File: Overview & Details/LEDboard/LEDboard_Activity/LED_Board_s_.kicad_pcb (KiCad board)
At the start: 2 copper layers, 0 parts

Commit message: Place components
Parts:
- added D1: APA102-2020, LED_SMD:LED-APA102-2020, F.Cu at (69.4, 47.9)
- added D10: APA102-2020, LED_SMD:LED-APA102-2020, F.Cu at (104.3, 57.5)
- added D11: APA102-2020, LED_SMD:LED-APA102-2020, F.Cu at (86.8, 57.5)
- added D12: APA102-2020, LED_SMD:LED-APA102-2020, F.Cu at (69.4, 57.5)
- added D13: APA102-2020, LED_SMD:LED-APA102-2020, F.Cu at (69.4, 67.0)
- added D14: APA102-2020, LED_SMD:LED-APA102-2020, F.Cu at (86.8, 67.0)
- added D15: APA102-2020, LED_SMD:LED-APA102-2020, F.Cu at (104.3, 67.0)
- added D16: APA102-2020, LED_SMD:LED-APA102-2020, F.Cu at (121.8, 67.0)
- added D17: APA102-2020, LED_SMD:LED-APA102-2020, F.Cu at (139.2, 67.0)
- added D18: APA102-2020, LED_SMD:LED-APA102-2020, F.Cu at (156.7, 67.0)
- added D19: APA102-2020, LED_SMD:LED-APA102-2020, F.Cu at (156.7, 76.5)
- added D2: APA102-2020, LED_SMD:LED-APA102-2020, F.Cu at (86.8, 47.9)
- added D20: APA102-2020, LED_SMD:LED-APA102-2020, F.Cu at (139.2, 76.5)
- added D21: APA102-2020, LED_SMD:LED-APA102-2020, F.Cu at (121.8, 76.5)
- added D22: APA102-2020, LED_SMD:LED-APA102-2020, F.Cu at (104.3, 76.5)
- added D23: APA102-2020, LED_SMD:LED-APA102-2020, F.Cu at (86.8, 76.5)
- added D24: APA102-2020, LED_SMD:LED-APA102-2020, F.Cu at (69.4, 76.5)
- added D25: APA102-2020, LED_SMD:LED-APA102-2020, F.Cu at (69.4, 86.0)
- added D26: APA102-2020, LED_SMD:LED-APA102-2020, F.Cu at (86.8, 86.0)
- added D27: APA102-2020, LED_SMD:LED-APA102-2020, F.Cu at (104.3, 86.0)
- added D28: APA102-2020, LED_SMD:LED-APA102-2020, F.Cu at (121.8, 86.0)
- added D29: APA102-2020, LED_SMD:LED-APA102-2020, F.Cu at (139.2, 86.0)
- added D3: APA102-2020, LED_SMD:LED-APA102-2020, F.Cu at (104.3, 47.9)
- added D30: APA102-2020, LED_SMD:LED-APA102-2020, F.Cu at (156.7, 86.0)
- added D31: APA102-2020, LED_SMD:LED-APA102-2020, F.Cu at (156.7, 95.6)
- added D32: APA102-2020, LED_SMD:LED-APA102-2020, F.Cu at (139.2, 95.6)
- added D33: APA102-2020, LED_SMD:LED-APA102-2020, F.Cu at (121.8, 95.6)
- added D34: APA102-2020, LED_SMD:LED-APA102-2020, F.Cu at (104.3, 95.6)
- added D35: APA102-2020, LED_SMD:LED-APA102-2020, F.Cu at (86.8, 95.6)
- added D36: APA102-2020, LED_SMD:LED-APA102-2020, F.Cu at (69.4, 95.6)
- added D37: APA102-2020, LED_SMD:LED-APA102-2020, F.Cu at (69.4, 105.1)
- added D38: APA102-2020, LED_SMD:LED-APA102-2020, F.Cu at (86.8, 105.1)
- added D39: APA102-2020, LED_SMD:LED-APA102-2020, F.Cu at (104.3, 105.1)
- added D4: APA102-2020, LED_SMD:LED-APA102-2020, F.Cu at (121.8, 47.9)
- added D40: APA102-2020, LED_SMD:LED-APA102-2020, F.Cu at (121.8, 105.1)
- added D41: APA102-2020, LED_SMD:LED-APA102-2020, F.Cu at (139.2, 105.1)
- added D42: APA102-2020, LED_SMD:LED-APA102-2020, F.Cu at (156.7, 105.1)
- added D43: APA102-2020, LED_SMD:LED-APA102-2020, F.Cu at (156.7, 114.6)
- added D44: APA102-2020, LED_SMD:LED-APA102-2020, F.Cu at (139.2, 114.6)
- added D45: APA102-2020, LED_SMD:LED-APA102-2020, F.Cu at (121.8, 114.6)
- added D46: APA102-2020, LED_SMD:LED-APA102-2020, F.Cu at (104.3, 114.6)
- added D47: APA102-2020, LED_SMD:LED-APA102-2020, F.Cu at (86.8, 114.6)
- added D48: APA102-2020, LED_SMD:LED-APA102-2020, F.Cu at (69.4, 114.6)
- added D5: APA102-2020, LED_SMD:LED-APA102-2020, F.Cu at (139.2, 47.9)
- added D6: APA102-2020, LED_SMD:LED-APA102-2020, F.Cu at (156.7, 47.9)
- added D7: APA102-2020, LED_SMD:LED-APA102-2020, F.Cu at (156.7, 57.5)
- added D8: APA102-2020, LED_SMD:LED-APA102-2020, F.Cu at (139.2, 57.5)
- added D9: APA102-2020, LED_SMD:LED-APA102-2020, F.Cu at (121.8, 57.5)
- added H1: MountingHole, MountingHole:MountingHole_3.5mm_Pad, F.Cu at (165.1, 114.3)
- added H2: MountingHole_Pad, MountingHole:MountingHole_3.5mm_Pad_Via, F.Cu at (61.0, 48.3)
- added H3: MountingHole, MountingHole:MountingHole_3.5mm_Pad, F.Cu at (165.1, 48.3)
- added H4: MountingHole, MountingHole:MountingHole_3.5mm_Pad, F.Cu at (61.0, 114.3)
- added J1: Conn_01x04, Connector_PinHeader_2.54mm:PinHeader_1x04_P2.54mm_Vertical, B.Cu at (61.0, 85.1)
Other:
- board outline added: 114.3 x 76.2 mm

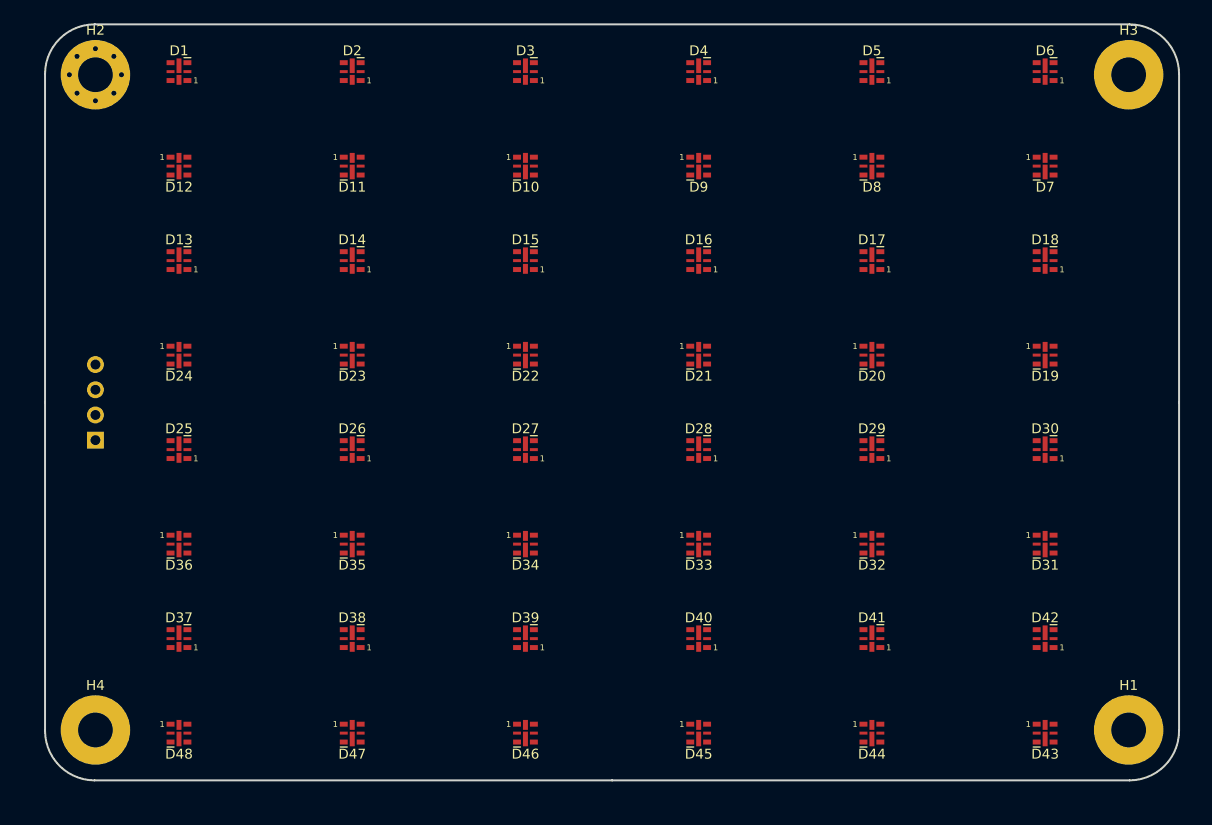
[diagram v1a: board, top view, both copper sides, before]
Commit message: add fiducials
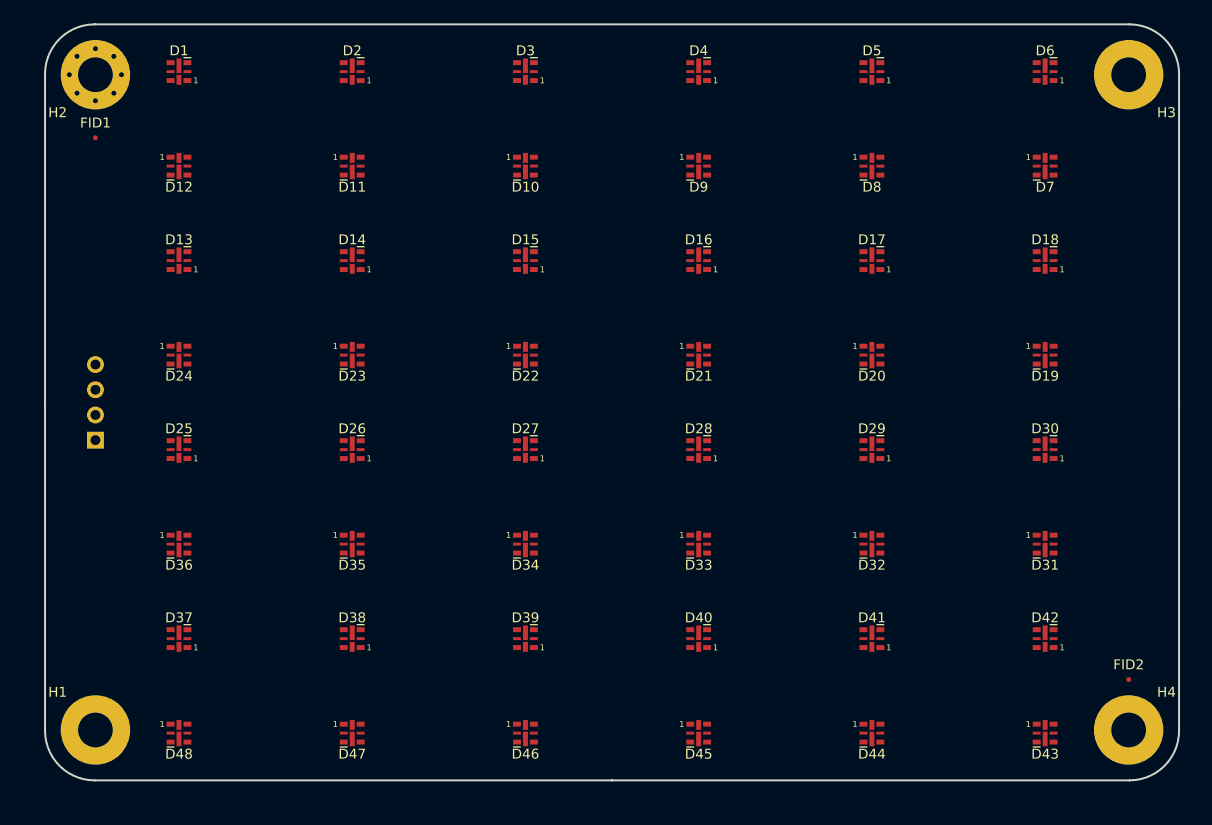
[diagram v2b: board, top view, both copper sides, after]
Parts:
- added FID1: Fiducial, Fiducial:Fiducial_0.5mm_Mask1mm, F.Cu at (61.0, 54.6)
- added FID2: Fiducial, Fiducial:Fiducial_0.5mm_Mask1mm, F.Cu at (165.1, 109.2)
- moved H1 104.1 mm to (61.0, 114.3)
- moved H4 104.1 mm to (165.1, 114.3)
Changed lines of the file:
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@@
     (tracks 0)
     (zones 0)
-    (modules 53)
+    (modules 55)
     (nets 101)
   )
@@
     (uvia_drill 0.1)
   )
+  (module Fiducial:Fiducial_0.5mm_Mask1mm (layer F.Cu)
+    (at 165.1 109.22)
+    (descr "Circular Fiducial, 0.5mm bare copper, 1mm soldermask opening (Level C)")
+    (tags fiducial)
+    (attr smd)
+    (fp_text reference FID2 (at 0 -1.5) (layer F.SilkS)
+      (effects (font (size 1 1) (thickness 0.15)))
+    )
+    (fp_text value Fiducial (at 11.43 1.27) (layer F.Fab) hide
+      (effects (font (size 1 1) (thickness 0.15)))
+    )
+    (fp_circle (center 0 0) (end 0.75 0) (layer F.CrtYd) (width 0.05))
+    (fp_text user %R (at 0 0) (layer F.Fab)
+      (effects (font (size 0.2 0.2) (thickness 0.04)))
+    )
+    (fp_circle (center 0 0) (end 0.5 0) (layer F.Fab) (width 0.1))
+    (pad "" smd circle (at 0 0) (size 0.5 0.5) (layers F.Cu F.Mask)
+      (solder_mask_margin 0.25) (clearance 0.25))
+  )
+  (module Fiducial:Fiducial_0.5mm_Mask1mm (layer F.Cu)
+    (at 60.96 54.61)
+    (descr "Circular Fiducial, 0.5mm bare copper, 1mm soldermask opening (Level C)")
+    (tags fiducial)
+    (attr smd)
+    (fp_text reference FID1 (at 0 -1.5) (layer F.SilkS)
+      (effects (font (size 1 1) (thickness 0.15)))
+    )
+    (fp_text value Fiducial (at 0 1.5) (layer F.Fab) hide
+      (effects (font (size 1 1) (thickness 0.15)))
+    )
+    (fp_circle (center 0 0) (end 0.75 0) (layer F.CrtYd) (width 0.05))
+    (fp_text user %R (at 0 0) (layer F.Fab)
+      (effects (font (size 0.2 0.2) (thickness 0.04)))
+    )
+    (fp_circle (center 0 0) (end 0.5 0) (layer F.Fab) (width 0.1))
+    (pad "" smd circle (at 0 0) (size 0.5 0.5) (layers F.Cu F.Mask)
+      (solder_mask_margin 0.25) (clearance 0.25))
+  )
   (module Connector_PinHeader_2.54mm:PinHeader_1x04_P2.54mm_Vertical (layer B.Cu)
     (at 60.96 85.09)
@@
   )
   (module MountingHole:MountingHole_3.5mm_Pad (layer F.Cu)
-    (at 60.96 114.3)
+    (at 165.1 114.3)
     (descr "Mounting Hole 3.5mm")
     (tags "mounting hole 3.5mm")
     (attr virtual)
-    (fp_text reference H4 (at 0 -4.5) (layer F.SilkS)
-      (effects (font (size 1 1) (thickness 0.15)))
-    )
-    (fp_text value MountingHole (at 0 4.5) (layer F.Fab)
+    (fp_text reference H4 (at 3.81 -3.81) (layer F.SilkS)
+      (effects (font (size 1 1) (thickness 0.15)))
+    )
+    (fp_text value MountingHole (at 0 4.5) (layer F.Fab) hide
       (effects (font (size 1 1) (thickness 0.15)))
     )
@@
     (tags "mounting hole 3.5mm")
     (attr virtual)
-    (fp_text reference H3 (at 0 -4.5) (layer F.SilkS)
-      (effects (font (size 1 1) (thickness 0.15)))
-    )
-    (fp_text value MountingHole (at 0 4.5) (layer F.Fab)
+    (fp_text reference H3 (at 3.81 3.81) (layer F.SilkS)
+      (effects (font (size 1 1) (thickness 0.15)))
+    )
+    (fp_text value MountingHole (at 3.81 -7.62) (layer F.Fab) hide
       (effects (font (size 1 1) (thickness 0.15)))
     )
@@
     (tags "mounting hole 3.5mm")
     (attr virtual)
-    (fp_text reference H2 (at 0 -4.5) (layer F.SilkS)
-      (effects (font (size 1 1) (thickness 0.15)))
-    )
-    (fp_text value MountingHole_Pad (at 0 4.5) (layer F.Fab)
+    (fp_text reference H2 (at -3.81 3.81) (layer F.SilkS)
+      (effects (font (size 1 1) (thickness 0.15)))
+    )
+    (fp_text value MountingHole_Pad (at -2.54 -8.89) (layer F.Fab) hide
       (effects (font (size 1 1) (thickness 0.15)))
     )
@@
   )
   (module MountingHole:MountingHole_3.5mm_Pad (layer F.Cu)
-    (at 165.1 114.3)
+    (at 60.96 114.3)
     (descr "Mounting Hole 3.5mm")
     (tags "mounting hole 3.5mm")
     (attr virtual)
-    (fp_text reference H1 (at 0 -4.5) (layer F.SilkS)
-      (effects (font (size 1 1) (thickness 0.15)))
-    )
-    (fp_text value MountingHole (at 0 4.5) (layer F.Fab)
-      (effects (font (size 1 1) (thickness 0.15)))
-    )
+    (fp_text reference H1 (at -3.81 -3.81) (layer F.SilkS)
+      (effects (font (size 1 1) (thickness 0.15)))
+    )
+    (fp_text value MountingHole (at 6.35 7.62) (layer F.Fab) hide
+      (effects (font (size 1 1) (thickness 0.15)))
+    )

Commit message: finish LEDboard PCB
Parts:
- moved FID1 2.84 mm to (58.4, 53.3)
- moved FID2 2.54 mm to (167.6, 109.2)
- moved H4 0.11 mm to (165.2, 114.4)
- moved H2 0.11 mm to (60.9, 48.2)
- moved H3 0.11 mm to (165.2, 48.2)
- moved H1 0.11 mm to (60.9, 114.4)
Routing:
- net +5VD: track 0.00 -> 202.3 mm
- net GND: track 0.00 -> 185.0 mm, vias 0 -> 200
- net /SDI: track 0.00 -> 44.0 mm
- net /CKI: track 0.00 -> 40.8 mm
- net Net-(D35-Pad2): track 0.00 -> 16.4 mm
- net Net-(D29-Pad3): track 0.00 -> 16.0 mm
- net Net-(D35-Pad3): track 0.00 -> 16.0 mm
- net Net-(D23-Pad3): track 0.00 -> 16.0 mm
- net Net-(D46-Pad2): track 0.00 -> 16.0 mm
- net Net-(D7-Pad3): track 0.00 -> 15.8 mm
- net Net-(D7-Pad2): track 0.00 -> 15.8 mm
- net Net-(D5-Pad3): track 0.00 -> 15.8 mm
- net Net-(D5-Pad2): track 0.00 -> 15.8 mm
- net Net-(D43-Pad3): track 0.00 -> 15.8 mm
- net Net-(D43-Pad2): track 0.00 -> 15.8 mm
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- added copper zone on F.Cu, net +5VD
- added copper zone on B.Cu, net GND
- added copper zone on F.Cu, net GND
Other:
- net class jlcpcb added: clearance 0.127, trace_width 0.25, via_dia 0.8, via_drill 0.4
- board text added: "Parthiv Krishna LEDboard / Spring 2020 / lab64 intro2PCBdesign workshop"

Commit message: add labels to connector
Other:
- board text added: "+5V"
- board text added: "CKI"
- board text added: "GND"
- board text added: "SDI"
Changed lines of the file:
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@@
   (general
     (thickness 1.6)
-    (drawings 12)
+    (drawings 16)
     (tracks 577)
     (zones 0)
@@
       (outputformat 1)
       (mirror false)
-      (drillshape 1)
+      (drillshape 0)
       (scaleselection 1)
-      (outputdirectory ""))
+      (outputdirectory "gerbers/"))
   )
   (net 0 "")
@@
     )
   )
+  (gr_text GND (at 63.5 85.09) (layer B.SilkS)
+    (effects (font (size 0.8 0.8) (thickness 0.12)) (justify mirror))
+  )
+  (gr_text SDI (at 63.5 82.55) (layer B.SilkS)
+    (effects (font (size 0.8 0.8) (thickness 0.12)) (justify mirror))
+  )
+  (gr_text CKI (at 63.5 80.01) (layer B.SilkS)
+    (effects (font (size 0.8 0.8) (thickness 0.12)) (justify mirror))
+  )
+  (gr_text +5V (at 63.5 77.47) (layer B.SilkS)
+    (effects (font (size 0.8 0.8) (thickness 0.12)) (justify mirror))
+  )
   (gr_text "Parthiv Krishna LEDboard / Spring 2020 / lab64 intro2PCBdesign workshop" (at 113.03 81.28) (layer F.SilkS)
